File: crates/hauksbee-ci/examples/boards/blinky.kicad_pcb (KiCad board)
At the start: 5 parts, among them U1 ATmega328P

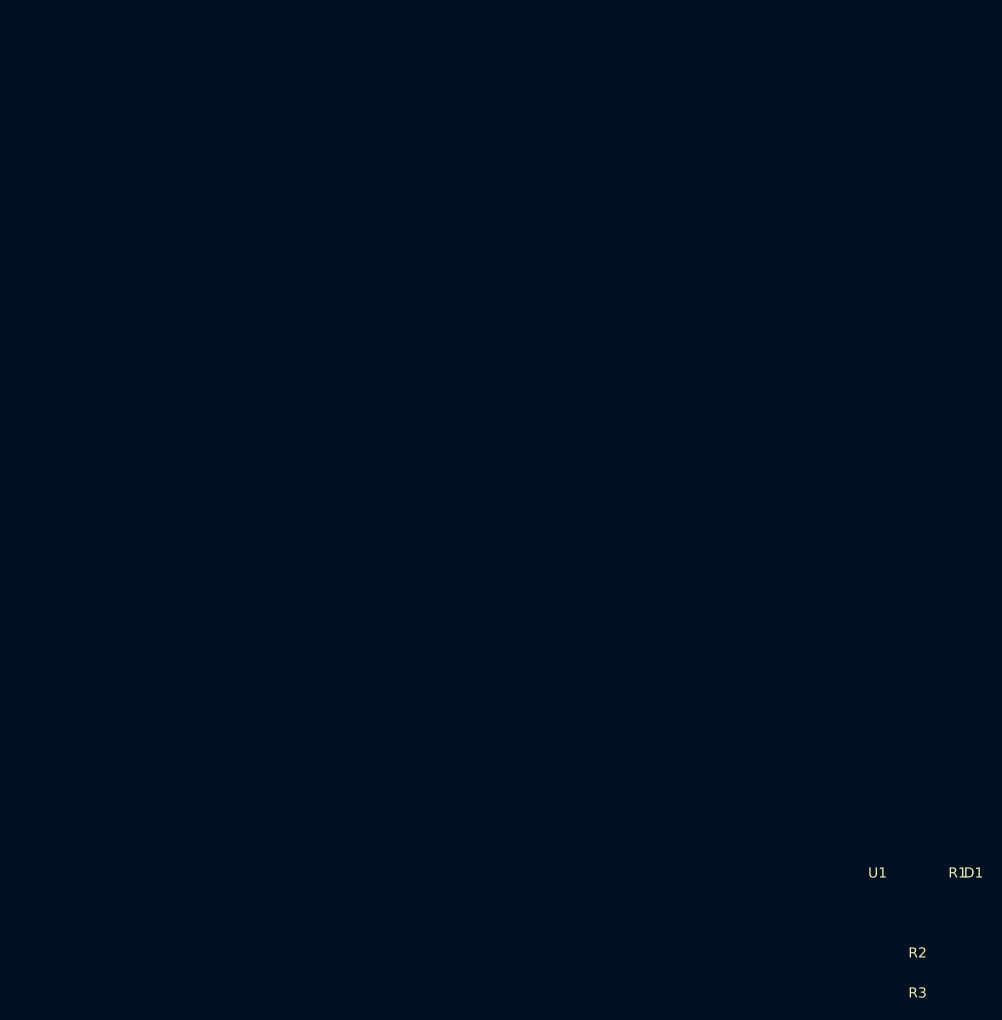
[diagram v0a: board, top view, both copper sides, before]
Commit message: Give the sample boards actual copper
blinky and boot_gate were pad-and-netlist fixtures with zero segments, zero
vias and no board outline, and they are two of the three boards the landing
page offers as one-click samples. A stranger's first click on a tool whose
whole claim is that it starts from the copper produced something that does not
look like a PCB.

Both are routed now, through hauksbee's own board-as-code plus freerouting
path, so repairing the samples exercised a shipped feature end to end. blinky
goes from 0 segments and no outline to 28 segments, an edge, 9 of 9
connections routed and 0 DRC violations. It binds identically: six parts, one
active IC, same verdict.

boot_gate is a judgement rather than a fix. Routing it clean is right for a
sample and wrong for a fixture: waiver_gate.rs asserts it gates red before any
waiver exists, and that premise is the only thing stopping the waiver tests
passing vacuously. Its two shorts come from overlapping pads rather than
traces, so the round-trip drops them. The sample copy is therefore the routed
clean board and the crate fixture keeps its faults, with the samples README
saying so instead of leaving the difference to be discovered.

Separately, the VCD sink failed with a bare "No such file or directory" when
its output path's parent did not exist, naming neither the path nor the
reason, after the simulation had already run. Naming an output under a
directory you have not created yet is an ordinary thing to do. It creates the
parent now. This predates the board change: it fails at HEAD too.
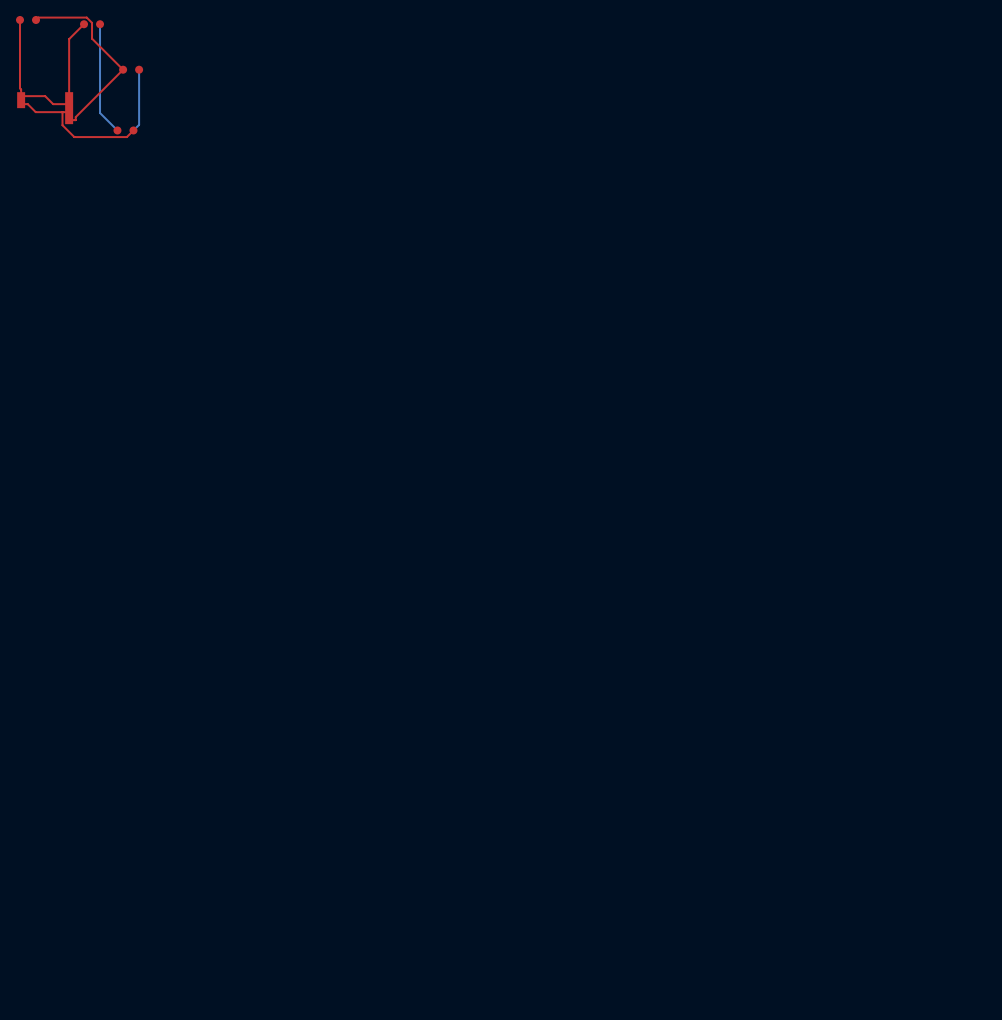
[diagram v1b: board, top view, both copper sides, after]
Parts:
- moved R2 161.8 mm to (-7.20, -6.61)
- moved R3 152.2 mm to (5.69, -0.39)
- moved R1 152.2 mm to (0.81, -6.08)
- moved U1 142.3 mm to (-4.06, 2.91)
- moved D1 141.6 mm to (4.99, 7.20)
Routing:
- net GND: track 0.00 -> 25.8 mm
- net ADC0: track 0.00 -> 24.4 mm
- net +5V: track 0.00 -> 16.0 mm
- net LED_A: track 0.00 -> 14.2 mm
- net D13: track 0.00 -> 9.76 mm
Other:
- copper layers 0 -> 2
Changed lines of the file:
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@@
-(kicad_pcb (version 20171130) (host pcbnew 5.1.0)
-  (net 0 "")
-  (net 1 "GND")
-  (net 2 "+5V")
-  (net 3 "D13")
-  (net 4 "LED_A")
-  (net 5 "ADC0")
-  (module Package_QFP:TQFP-32_7x7mm_P0.8mm (layer F.Cu)
-    (at 100 100)
-    (fp_text reference U1 (at 0 0) (layer F.SilkS))
-    (fp_text value ATmega328P (at 0 2) (layer F.Fab))
-    (pad 7  smd rect (at -3 0) (net 2 "+5V"))
-    (pad 8  smd rect (at -3 1) (net 1 "GND"))
-    (pad 19 smd rect (at 3 0) (net 3 "D13"))
-    (pad 20 smd rect (at 3 1) (net 2 "+5V"))
-    (pad 22 smd rect (at 3 2) (net 1 "GND"))
-    (pad 23 smd rect (at 3 3) (net 5 "ADC0"))
-  )
-  (module Resistor_THT:R_Axial_DIN0207_L6.3mm_D2.5mm (layer F.Cu)
-    (at 110 100)
-    (fp_text reference R1 (at 0 0) (layer F.SilkS))
-    (fp_text value 330 (at 0 2) (layer F.Fab))
-    (pad 1 thru_hole circle (at 0 0) (net 3 "D13"))
-    (pad 2 thru_hole circle (at 2 0) (net 4 "LED_A"))
-  )
-  (module LED_THT:LED_D5.0mm (layer F.Cu)
-    (at 112 100)
-    (fp_text reference D1 (at 0 0) (layer F.SilkS))
-    (fp_text value RED_LED (at 0 2) (layer F.Fab))
-    (pad A thru_hole circle (at 0 0) (net 4 "LED_A"))
-    (pad K thru_hole circle (at 2 0) (net 1 "GND"))
-  )
-  (module Resistor_THT:R_Axial_DIN0207_L6.3mm_D2.5mm (layer F.Cu)
-    (at 105 110)
-    (fp_text reference R2 (at 0 0) (layer F.SilkS))
-    (fp_text value 10k (at 0 2) (layer F.Fab))
-    (pad 1 thru_hole circle (at 0 0) (net 2 "+5V"))
-    (pad 2 thru_hole circle (at 2 0) (net 5 "ADC0"))
-  )
-  (module Resistor_THT:R_Axial_DIN0207_L6.3mm_D2.5mm (layer F.Cu)
-    (at 105 115)
-    (fp_text reference R3 (at 0 0) (layer F.SilkS))
-    (fp_text value 10k (at 0 2) (layer F.Fab))
-    (pad 1 thru_hole circle (at 0 0) (net 5 "ADC0"))
-    (pad 2 thru_hole circle (at 2 0) (net 1 "GND"))
-  )
-)
+(kicad_pcb(version 20171130)(generator "pcbnew")(general(thickness 1.6))(paper "A4")(layers(0 "F.Cu"signal)(31 "B.Cu"signal)(36 "B.SilkS"user)(37 "F.SilkS"user)(38 "B.Mask"user)(39 "F.Mask"user)(44 "Edge.Cuts"user)(48 "B.Fab"user)(49 "F.Fab"user))(setup(pad_to_mask_clearance 0))(net 0 "")(net 1 "+5V")(net 2 "GND")(net 3 "D13")(net 4 "ADC0")(net 5 "LED_A")(footprint "Resistor_THT:R_Axial_DIN0207_L6.3mm_D2.5mm"(layer "F.Cu")(at -7.198 -6.605 0)(property "Reference""R2")(property "Value""10k")(pad 1 thru_hole circle(at 0 0 0)(size 1 1)(layers "F.Cu")(net 1 "+5V"))(pad 2 thru_hole circle(at 2 0 0)(size 1 1)(layers "F.Cu")(net 4 "ADC0")))(footprint "Resistor_THT:R_Axial_DIN0207_L6.3mm_D2.5mm"(layer "F.Cu")(at 5.69 -0.389 0)(property "Reference""R3")(property "Value""10k")(pad 1 thru_hole circle(at 0 0 0)(size 1 1)(layers "F.Cu")(net 4 "ADC0"))(pad 2 thru_hole circle(at 2 0 0)(size 1 1)(layers "F.Cu")(net 2 "GND")))(footprint "LED_THT:LED_D5.0mm"(layer "F.Cu")(at 4.988 7.204 0)(property "Reference""D1")(property "Value""RED_LED")(pad A thru_hole circle(at 0 0 0)(size 1 1)(layers "F.Cu")(net 5 "LED_A"))(pad K thru_hole circle(at 2 0 0)(size 1 1)(layers "F.Cu")(net 2 "GND")))(footprint "Package_QFP:TQFP-32_7x7mm_P0.8mm"(layer "F.Cu")(at -4.056 2.913 0)(property "Reference""U1")(property "Value""ATmega328P")(pad 7 smd rect(at -3 0 0)(size 1 1)(layers "F.Cu")(net 1 "+5V"))(pad 8 smd rect(at -3 1 0)(size 1 1)(layers "F.Cu")(net 2 "GND"))(pad 19 smd rect(at 3 0 0)(size 1 1)(layers "F.Cu")(net 3 "D13"))(pad 20 smd rect(at 3 1 0)(size 1 1)(layers "F.Cu")(net 1 "+5V"))(pad 22 smd rect(at 3 2 0)(size 1 1)(layers "F.Cu")(net 2 "GND"))(pad 23 smd rect(at 3 3 0)(size 1 1)(layers "F.Cu")(net 4 "ADC0")))(footprint "Resistor_THT:R_Axial_DIN0207_L6.3mm_D2.5mm"(layer "F.Cu")(at 0.805 -6.076 0)(property "Reference""R1")(property "Value""330")(pad 1 thru_hole circle(at 0 0 0)(size 1 1)(layers "F.Cu")(net 3 "D13"))(pad 2 thru_hole circle(at 2 0 0)(size 1 1)(layers "F.Cu")(net 5 "LED_A")))(segment(start -7.056 2.913)(end -7.056 2.08783)(width 0.25)(layer "F.Cu")(net 1))(segment(start -7.056 2.08783)(end -7.198 1.94583)(width 0.25)(layer "F.Cu")(net 1))(segment(start -7.198 1.94583)(end -7.198 -6.605)(width 0.25)(layer "F.Cu")(net 1))(segment(start -1.056 3.913)(end -3.04992 3.913)(width 0.25)(layer "F.Cu")(net 1))(segment(start -3.04992 3.913)(end -4.04992 2.913)(width 0.25)(layer "F.Cu")(net 1))(segment(start -4.04992 2.913)(end -7.056 2.913)(width 0.25)(layer "F.Cu")(net 1))(segment(start 5.69 -0.389)(end 1.805 -4.274)(width 0.25)(layer "F.Cu")(net 4))(segment(start 1.805 -4.274)(end 1.805 -6.24772)(width 0.25)(layer "F.Cu")(net 4))(segment(start 1.805 -6.24772)(end 1.14557 -6.90715)(width 0.25)(layer "F.Cu")(net 4))(segment(start 1.14557 -6.90715)(end -4.89585 -6.90715)(width 0.25)(layer "F.Cu")(net 4))(segment(start -4.89585 -6.90715)(end -5.198 -6.605)(width 0.25)(layer "F.Cu")(net 4))(segment(start -1.056 5.913)(end -0.23083 5.913)(width 0.25)(layer "F.Cu")(net 4))(segment(start -0.23083 5.913)(end -0.23083 5.53183)(width 0.25)(layer "F.Cu")(net 4))(segment(start -0.23083 5.53183)(end 5.69 -0.389)(width 0.25)(layer "F.Cu")(net 4))(segment(start 0.805 -6.076)(end -1.056 -4.215)(width 0.25)(layer "F.Cu")(net 3))(segment(start -1.056 -4.215)(end -1.056 2.913)(width 0.25)(layer "F.Cu")(net 3))(segment(start 6.988 7.204)(end 7.69 6.502)(width 0.25)(layer "B.Cu")(net 2))(segment(start 7.69 6.502)(end 7.69 -0.389)(width 0.25)(layer "B.Cu")(net 2))(segment(start -1.886 4.913)(end -5.23083 4.913)(width 0.25)(layer "F.Cu")(net 2))(segment(start -5.23083 4.913)(end -6.23083 3.913)(width 0.25)(layer "F.Cu")(net 2))(segment(start -1.056 4.913)(end -1.886 4.913)(width 0.25)(layer "F.Cu")(net 2))(segment(start -1.886 4.913)(end -1.886 6.54883)(width 0.25)(layer "F.Cu")(net 2))(segment(start -1.886 6.54883)(end -0.40545 8.02938)(width 0.25)(layer "F.Cu")(net 2))(segment(start -0.40545 8.02938)(end 6.16262 8.02938)(width 0.25)(layer "F.Cu")(net 2))(segment(start 6.16262 8.02938)(end 6.988 7.204)(width 0.25)(layer "F.Cu")(net 2))(segment(start -7.056 3.913)(end -6.23083 3.913)(width 0.25)(layer "F.Cu")(net 2))(segment(start 2.805 -6.076)(end 2.805 5.021)(width 0.25)(layer "B.Cu")(net 5))(segment(start 2.805 5.021)(end 4.988 7.204)(width 0.25)(layer "B.Cu")(net 5)))
